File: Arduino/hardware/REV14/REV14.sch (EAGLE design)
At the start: 23 parts, among them IC2 ATMEGA168-AU, Q1 32768Hz, U1 RN2483, U4 SHT21, X1 SMA-142-0701-881/886, X2 SMA-142-0701-881/886

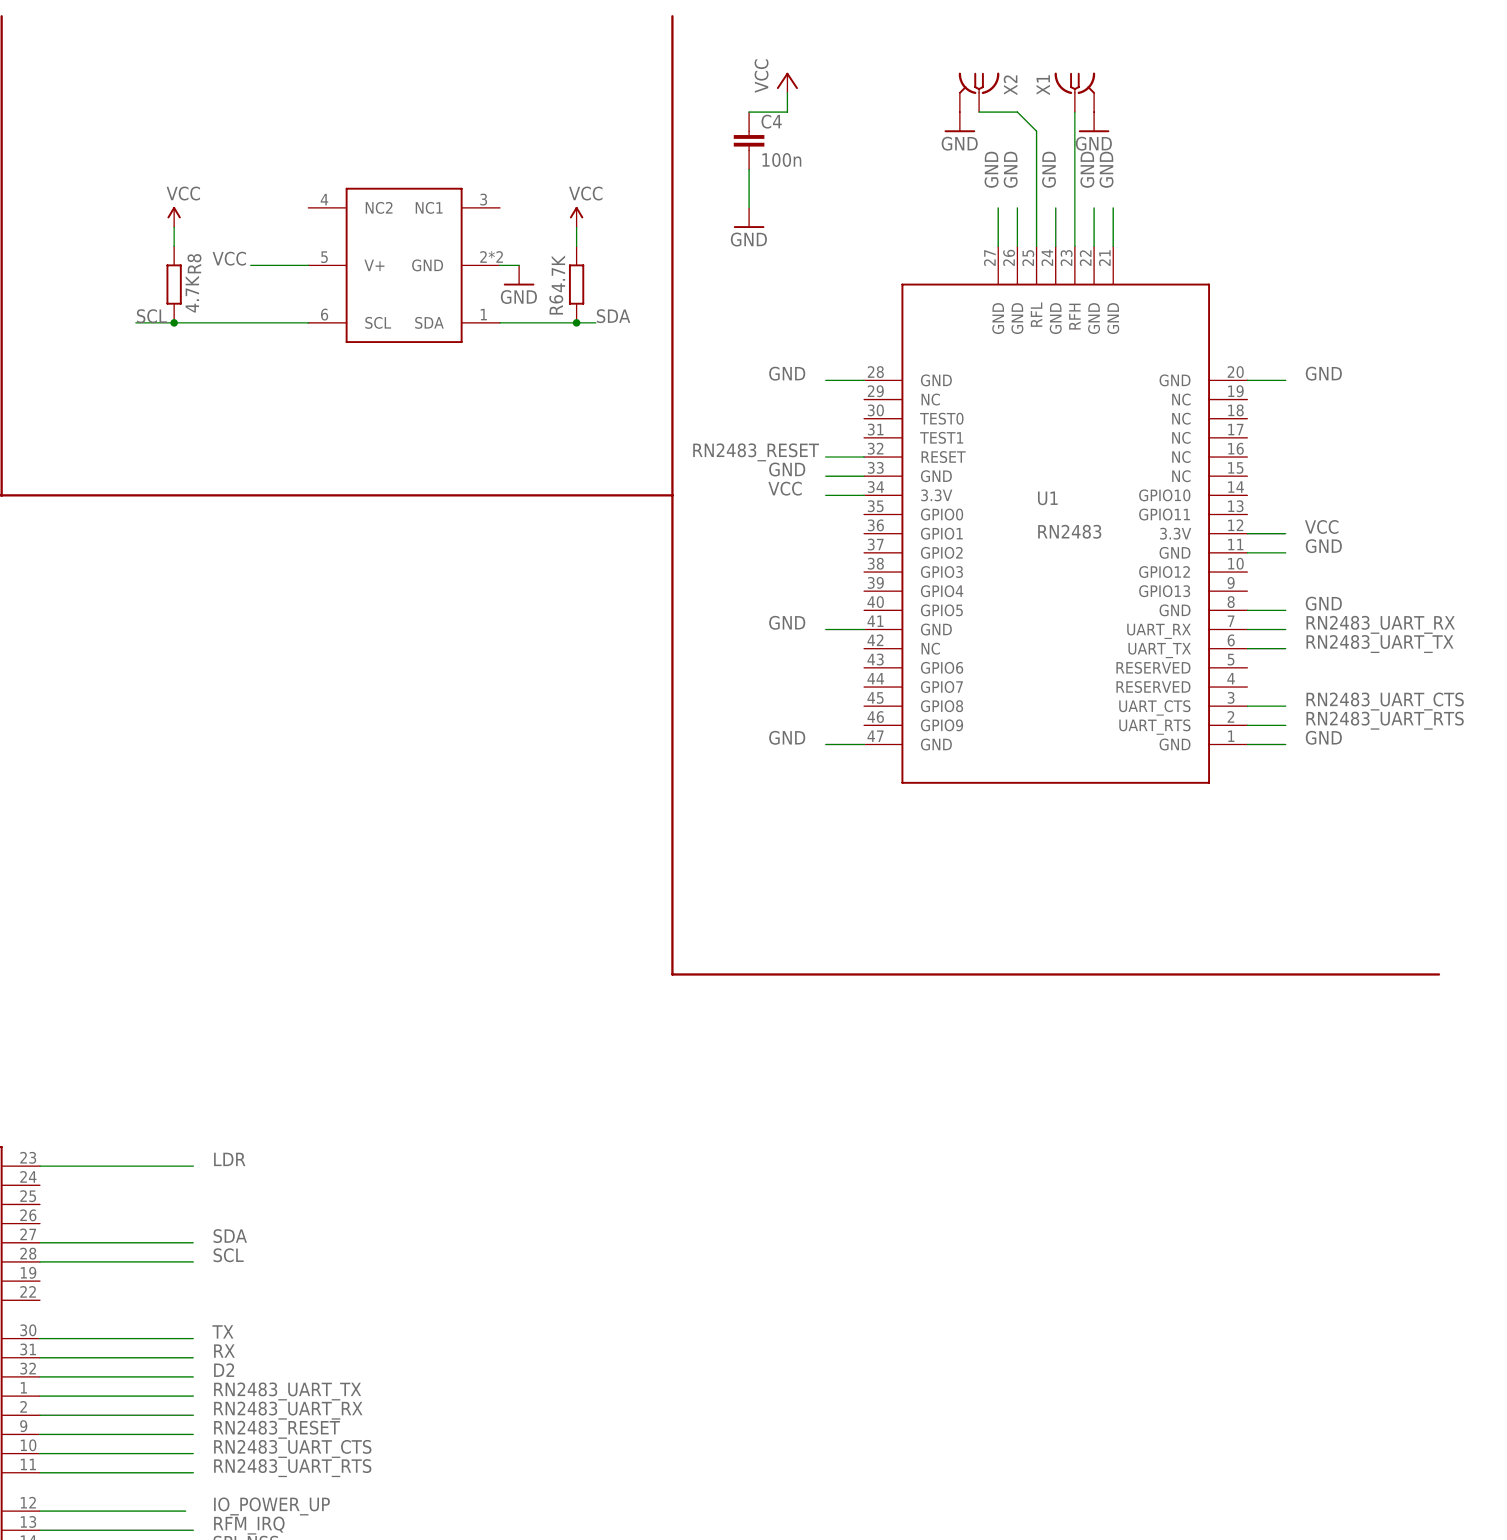
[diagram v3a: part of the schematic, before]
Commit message: added ftdi for updating LoRa
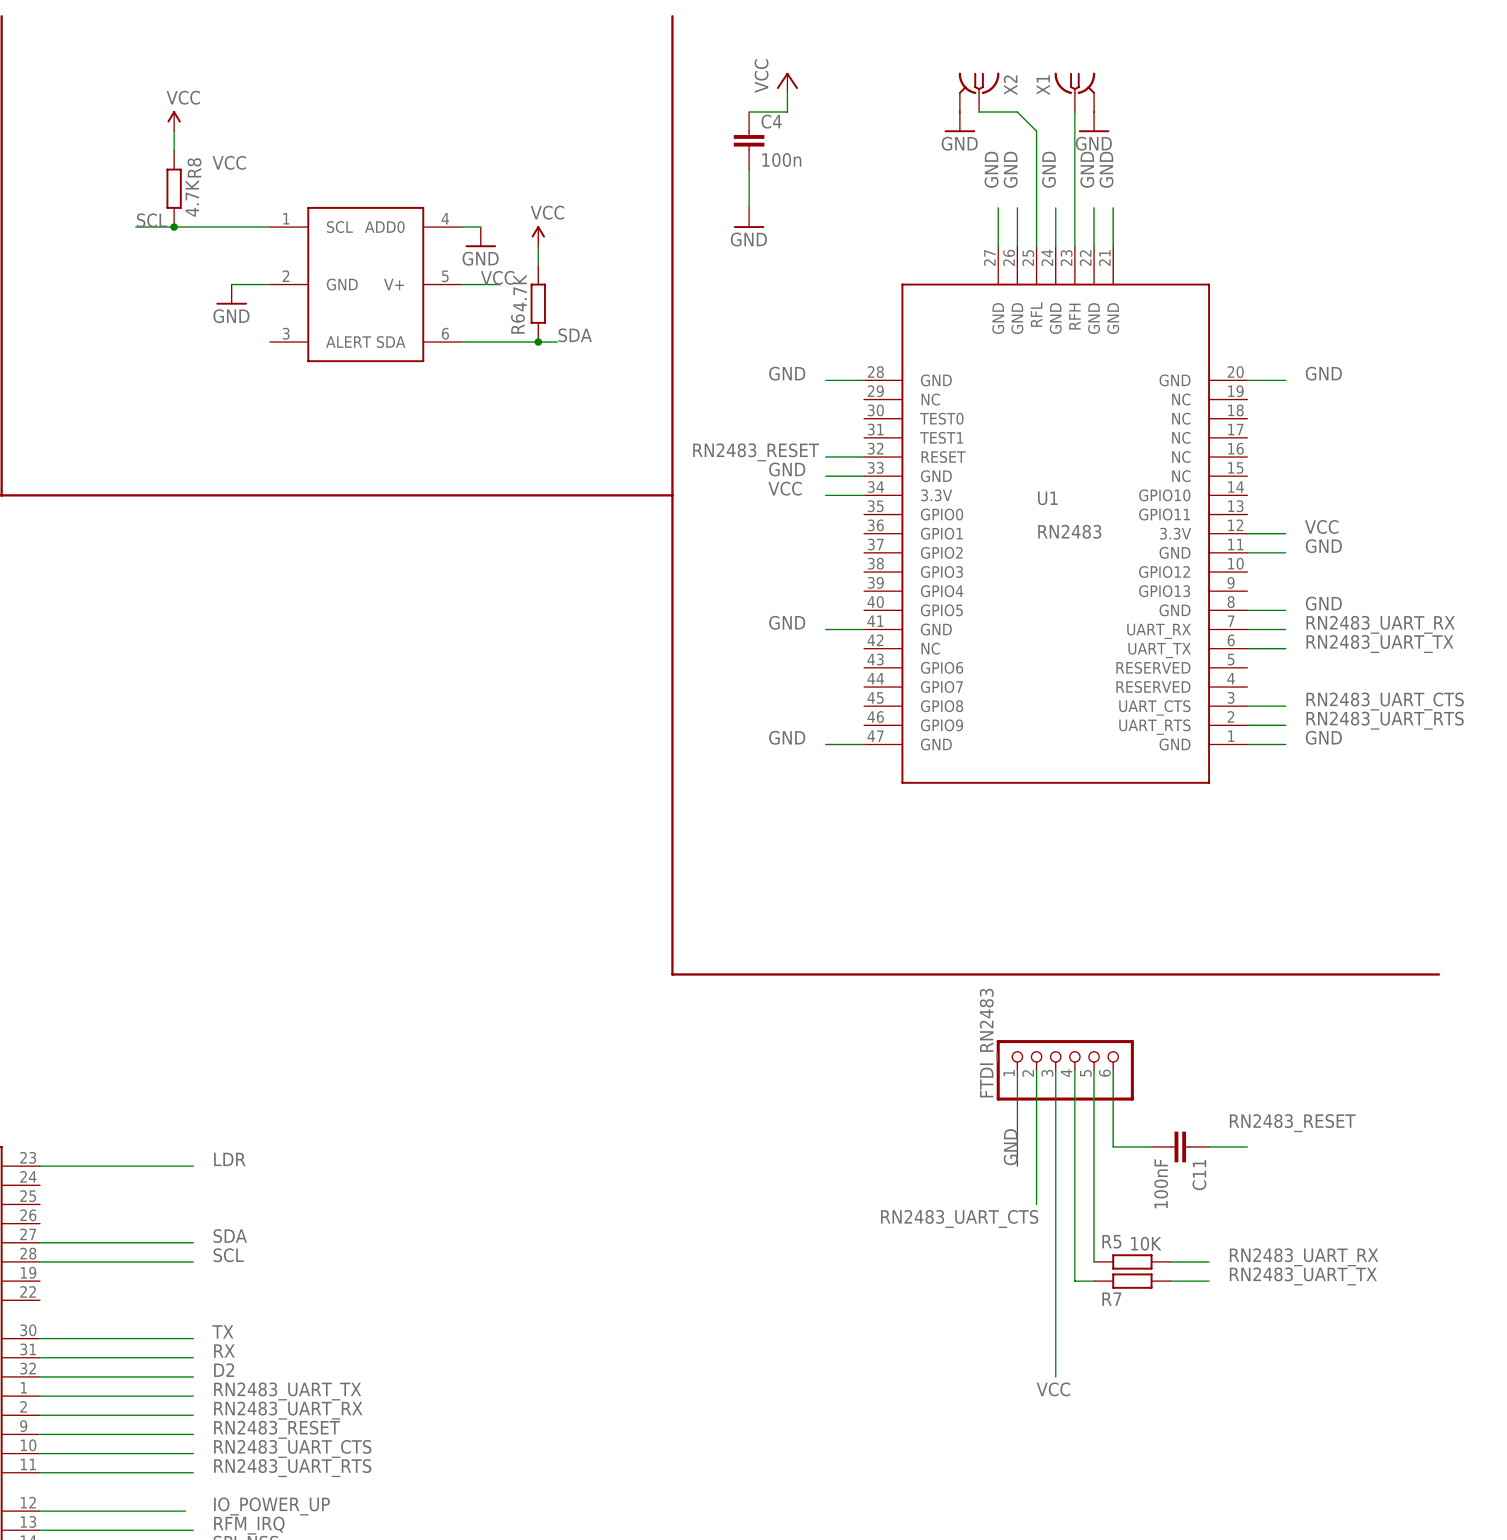
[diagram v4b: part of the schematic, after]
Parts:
- removed U4: SHT21, SHT21:SHT21
- added C11: 100nF, resistor:C-EUC0603
- added FTDI_RN2483: (no value), pinhead:PINHD-1X6
- added R5, R7: 10K, resistor:R-EU_R0603
- added U2: TMP112, TMP112_2:TMP112
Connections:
- new net N$2: C11.2, FTDI_RN2483.6
- new net N$5: FTDI_RN2483.4, R7.2
- new net N$7: FTDI_RN2483.5, R5.2
- net GND: now also FTDI_RN2483.1, U2.ADD0, U2.GND; no longer U4.GND
- net RN2483_RESET: now also C11.1
- net RN2483_UART_CTS: now also FTDI_RN2483.2
- net RN2483_UART_RX: now also R5.1
- net RN2483_UART_TX: now also R7.1
- net SCL: now also U2.SCL; no longer U4.SCL
- net SDA: now also U2.SDA; no longer U4.SDA
- net VCC: now also FTDI_RN2483.3, U2.V+; no longer U4.V+
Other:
- moved on the sheet: R6, R8
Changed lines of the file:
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@@
 <part name="P+1" library="SparkFun-Aesthetics" deviceset="VCC" device=""/>
 <part name="P+4" library="SparkFun-Aesthetics" deviceset="VCC" device=""/>
-<part name="U4" library="SHT21" deviceset="SHT21" device=""/>
 <part name="GND2" library="SparkFun-Aesthetics" deviceset="GND" device=""/>
 <part name="R1" library="resistor" deviceset="R-EU_" device="R0603" value="100K"/>
@@
 <part name="GND4" library="supply1" deviceset="GND" device=""/>
 <part name="GND5" library="supply1" deviceset="GND" device=""/>
+<part name="U2" library="TMP112_2" deviceset="TMP112" device=""/>
+<part name="GND7" library="SparkFun-Aesthetics" deviceset="GND" device=""/>
+<part name="R5" library="resistor" deviceset="R-EU_" device="R0603" value="10K"/>
+<part name="R7" library="resistor" deviceset="R-EU_" device="R0603" value="10K"/>
+<part name="C11" library="resistor" deviceset="C-EU" device="C0603" value="100nF"/>
+<part name="FTDI_RN2483" library="pinhead" deviceset="PINHD-1X6" device=""/>
 </parts>
 <sheets>
@@
 <instance part="C12" gate="G$1" x="134.62" y="63.5"/>
 <instance part="IC2" gate="1" x="167.64" y="76.2"/>
-<instance part="GND1" gate="1" x="261.62" y="220.98"/>
-<instance part="R6" gate="G$1" x="269.24" y="220.98" smashed="yes" rot="R270">
-<attribute name="NAME" x="265.6586" y="219.71" size="1.778" layer="95" rot="R270"/>
-<attribute name="VALUE" x="265.938" y="224.79" size="1.778" layer="96" rot="R270"/>
-</instance>
-<instance part="R8" gate="G$1" x="215.9" y="220.98" smashed="yes" rot="R90">
-<attribute name="NAME" x="219.4814" y="222.25" size="1.778" layer="95" rot="R90"/>
-<attribute name="VALUE" x="219.202" y="217.17" size="1.778" layer="96" rot="R90"/>
-</instance>
-<instance part="P+1" gate="G$1" x="215.9" y="228.6"/>
-<instance part="P+4" gate="G$1" x="269.24" y="228.6"/>
-<instance part="U4" gate="G$1" x="246.38" y="223.52"/>
+<instance part="GND1" gate="1" x="256.54" y="226.06"/>
+<instance part="R6" gate="G$1" x="264.16" y="218.44" smashed="yes" rot="R270">
+<attribute name="NAME" x="260.5786" y="217.17" size="1.778" layer="95" rot="R270"/>
+<attribute name="VALUE" x="260.858" y="222.25" size="1.778" layer="96" rot="R270"/>
+</instance>
+<instance part="R8" gate="G$1" x="215.9" y="233.68" smashed="yes" rot="R90">
+<attribute name="NAME" x="219.4814" y="234.95" size="1.778" layer="95" rot="R90"/>
+<attribute name="VALUE" x="219.202" y="229.87" size="1.778" layer="96" rot="R90"/>
+</instance>
+<instance part="P+1" gate="G$1" x="215.9" y="241.3"/>
+<instance part="P+4" gate="G$1" x="264.16" y="226.06"/>
 <instance part="GND2" gate="1" x="63.5" y="228.6"/>
 <instance part="R1" gate="G$1" x="71.12" y="231.14" rot="R180"/>
@@
 <instance part="GND4" gate="1" x="320.04" y="241.3"/>
 <instance part="GND5" gate="1" x="337.82" y="241.3"/>
+<instance part="U2" gate="G$1" x="241.3" y="220.98"/>
+<instance part="GND7" gate="1" x="223.52" y="218.44"/>
+<instance part="R5" gate="G$1" x="342.9" y="91.44" smashed="yes" rot="R180">
+<attribute name="NAME" x="341.63" y="95.0214" size="1.778" layer="95" rot="R180"/>
+<attribute name="VALUE" x="346.71" y="94.742" size="1.778" layer="96" rot="R180"/>
+</instance>
+<instance part="R7" gate="G$1" x="342.9" y="88.9" smashed="yes" rot="R180">
+<attribute name="NAME" x="341.63" y="87.4014" size="1.778" layer="95" rot="R180"/>
+</instance>
+<instance part="C11" gate="G$1" x="350.52" y="106.68" rot="R270"/>
+<instance part="FTDI_RN2483" gate="A" x="335.28" y="119.38" rot="R90"/>
 </instances>
 <busses>
@@
 <segment>
 <pinref part="GND1" gate="1" pin="GND"/>
-<wire x1="259.08" y1="223.52" x2="261.62" y2="223.52" width="0.1524" layer="91"/>
-<pinref part="U4" gate="G$1" pin="GND"/>
+<wire x1="254" y1="228.6" x2="256.54" y2="228.6" width="0.1524" layer="91"/>
+<pinref part="U2" gate="G$1" pin="ADD0"/>
 </segment>
 <segment>
@@
 <pinref part="X1" gate="G1" pin="2"/>
 <pinref part="GND5" gate="1" pin="GND"/>
+</segment>
+<segment>
+<pinref part="GND7" gate="1" pin="GND"/>
+<wire x1="228.6" y1="220.98" x2="223.52" y2="220.98" width="0.1524" layer="91"/>
+<pinref part="U2" gate="G$1" pin="GND"/>
+</segment>
+<segment>
+<wire x1="327.66" y1="116.84" x2="327.66" y2="104.14" width="0.1524" layer="91"/>
+<label x="327.66" y="104.14" size="1.778" layer="95" rot="R90"/>
+<pinref part="FTDI_RN2483" gate="A" pin="1"/>
 </segment>
 </net>
@@
 </segment>
 <segment>
-<wire x1="233.68" y1="223.52" x2="226.06" y2="223.52" width="0.1524" layer="91"/>
-<label x="220.98" y="223.52" size="1.778" layer="95"/>
-<pinref part="U4" gate="G$1" pin="V+"/>
+<wire x1="259.08" y1="220.98" x2="254" y2="220.98" width="0.1524" layer="91"/>
+<label x="220.98" y="236.22" size="1.778" layer="95"/>
+<label x="256.54" y="220.98" size="1.778" layer="95"/>
+<pinref part="U2" gate="G$1" pin="V+"/>
 </segment>
 <segment>
 <pinref part="R8" gate="G$1" pin="2"/>
 <pinref part="P+1" gate="G$1" pin="VCC"/>
-<wire x1="215.9" y1="226.06" x2="215.9" y2="228.6" width="0.1524" layer="91"/>
+<wire x1="215.9" y1="238.76" x2="215.9" y2="241.3" width="0.1524" layer="91"/>
 </segment>
 <segment>
 <pinref part="R6" gate="G$1" pin="1"/>
 <pinref part="P+4" gate="G$1" pin="VCC"/>
-<wire x1="269.24" y1="226.06" x2="269.24" y2="228.6" width="0.1524" layer="91"/>
+<wire x1="264.16" y1="223.52" x2="264.16" y2="226.06" width="0.1524" layer="91"/>
 </segment>
 <segment>
@@
 <pinref part="I2C_EXT" gate="A" pin="2"/>
 </segment>
+<segment>
+<wire x1="332.74" y1="116.84" x2="332.74" y2="76.2" width="0.1524" layer="91"/>
+<pinref part="FTDI_RN2483" gate="A" pin="3"/>
+<label x="330.2" y="73.66" size="1.778" layer="95"/>
+</segment>
 </net>
 <net name="SPI_SCK" class="0">
@@
 </segment>
 <segment>
-<wire x1="259.08" y1="215.9" x2="269.24" y2="215.9" width="0.1524" layer="91"/>
-<label x="271.78" y="215.9" size="1.778" layer="95"/>
+<wire x1="254" y1="213.36" x2="264.16" y2="213.36" width="0.1524" layer="91"/>
+<label x="266.7" y="213.36" size="1.778" layer="95"/>
 <pinref part="R6" gate="G$1" pin="2"/>
-<wire x1="269.24" y1="215.9" x2="271.78" y2="215.9" width="0.1524" layer="91"/>
-<junction x="269.24" y="215.9"/>
-<pinref part="U4" gate="G$1" pin="SDA"/>
+<wire x1="264.16" y1="213.36" x2="266.7" y2="213.36" width="0.1524" layer="91"/>
+<junction x="264.16" y="213.36"/>
+<pinref part="U2" gate="G$1" pin="SDA"/>
 </segment>
 <segment>
@@
 </segment>
 <segment>
-<wire x1="210.82" y1="215.9" x2="215.9" y2="215.9" width="0.1524" layer="91"/>
-<label x="210.82" y="215.9" size="1.778" layer="95"/>
+<wire x1="210.82" y1="228.6" x2="215.9" y2="228.6" width="0.1524" layer="91"/>
+<label x="210.82" y="228.6" size="1.778" layer="95"/>
 <pinref part="R8" gate="G$1" pin="1"/>
-<wire x1="215.9" y1="215.9" x2="233.68" y2="215.9" width="0.1524" layer="91"/>
-<junction x="215.9" y="215.9"/>
-<pinref part="U4" gate="G$1" pin="SCL"/>
+<wire x1="215.9" y1="228.6" x2="228.6" y2="228.6" width="0.1524" layer="91"/>
+<junction x="215.9" y="228.6"/>
+<pinref part="U2" gate="G$1" pin="SCL"/>
 </segment>
 <segment>
@@
 <pinref part="U1" gate="G$1" pin="UART_TX"/>
 </segment>
+<segment>
+<wire x1="347.98" y1="88.9" x2="353.06" y2="88.9" width="0.1524" layer="91"/>
+<label x="355.6" y="88.9" size="1.778" layer="95"/>
+<pinref part="R7" gate="G$1" pin="1"/>
+</segment>
 </net>
 <net name="RN2483_UART_RX" class="0">
@@
 <pinref part="U1" gate="G$1" pin="UART_RX"/>
 </segment>
+<segment>
+<wire x1="347.98" y1="91.44" x2="353.06" y2="91.44" width="0.1524" layer="91"/>
+<label x="355.6" y="91.44" size="1.778" layer="95"/>
+<pinref part="R5" gate="G$1" pin="1"/>
+</segment>
 </net>
 <net name="RN2483_RESET" class="0">
@@
 <pinref part="U1" gate="G$1" pin="RESET"/>
 </segment>
+<segment>
+<wire x1="353.06" y1="106.68" x2="358.14" y2="106.68" width="0.1524" layer="91"/>
+<label x="355.6" y="109.22" size="1.778" layer="95"/>
+<pinref part="C11" gate="G$1" pin="1"/>
+</segment>
 </net>
 <net name="N$1" class="0">
@@
 <label x="365.76" y="165.1" size="1.778" layer="95"/>
 <pinref part="U1" gate="G$1" pin="UART_CTS"/>
+</segment>
+<segment>
+<wire x1="330.2" y1="116.84" x2="330.2" y2="99.06" width="0.1524" layer="91"/>
+<label x="309.372" y="96.52" size="1.778" layer="95"/>
+<pinref part="FTDI_RN2483" gate="A" pin="2"/>
 </segment>
 </net>
@@
 </segment>
 </net>
+<net name="N$2" class="0">
+<segment>
+<wire x1="340.36" y1="116.84" x2="340.36" y2="106.68" width="0.1524" layer="91"/>
+<wire x1="340.36" y1="106.68" x2="345.44" y2="106.68" width="0.1524" layer="91"/>
+<pinref part="C11" gate="G$1" pin="2"/>
+<pinref part="FTDI_RN2483" gate="A" pin="6"/>
+</segment>
+</net>
+<net name="N$5" class="0">
+<segment>
+<pinref part="R7" gate="G$1" pin="2"/>
+<wire x1="335.28" y1="116.84" x2="335.28" y2="88.9" width="0.1524" layer="91"/>
+<wire x1="335.28" y1="88.9" x2="337.82" y2="88.9" width="0.1524" layer="91"/>
+<pinref part="FTDI_RN2483" gate="A" pin="4"/>
+</segment>
+</net>
+<net name="N$7" class="0">
+<segment>
+<pinref part="R5" gate="G$1" pin="2"/>
+<wire x1="337.82" y1="116.84" x2="337.82" y2="91.44" width="0.1524" layer="91"/>
+<pinref part="FTDI_RN2483" gate="A" pin="5"/>
+</segment>
+</net>

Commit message: rev 14 updated and intial routing attempt
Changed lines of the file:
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@@
 <wire x1="139.7" y1="157.48" x2="139.7" y2="193.04" width="0.3048" layer="94"/>
 <wire x1="104.14" y1="157.48" x2="139.954" y2="157.48" width="0.3048" layer="94"/>
-<wire x1="281.94" y1="129.54" x2="281.94" y2="193.04" width="0.3048" layer="94"/>
+<wire x1="281.94" y1="129.54" x2="281.94" y2="132.08" width="0.3048" layer="94"/>
+<wire x1="281.94" y1="132.08" x2="281.94" y2="193.04" width="0.3048" layer="94"/>
 <wire x1="281.94" y1="129.54" x2="383.54" y2="129.54" width="0.3048" layer="94"/>
 <text x="124.46" y="233.68" size="1.778" layer="94">On BOM</text>
 <text x="132.08" y="233.68" size="1.778" layer="94" rot="R270">On BOM</text>
+<wire x1="281.94" y1="68.58" x2="383.54" y2="68.58" width="0.3048" layer="94"/>
+<wire x1="281.94" y1="68.58" x2="281.94" y2="132.08" width="0.3048" layer="94"/>
 </plain>
 <instances>
